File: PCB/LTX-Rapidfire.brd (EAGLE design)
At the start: 46.7 x 62.2 mm, 51 parts, among them J1 F-1X08-SIP-100-40Y, Q1 2N3904, Q10 SS8550D, Q11 2N3906, Q12 2N3906, Q13 2N3904, Q2 2N3906, Q3 2N3904, Q4 2N3904, Q5 2N3904, Q6 2N3906, Q7 2N3906, Q8 2N3906, Q9 2N3904, SW1 F-1X02-SIP-100-40

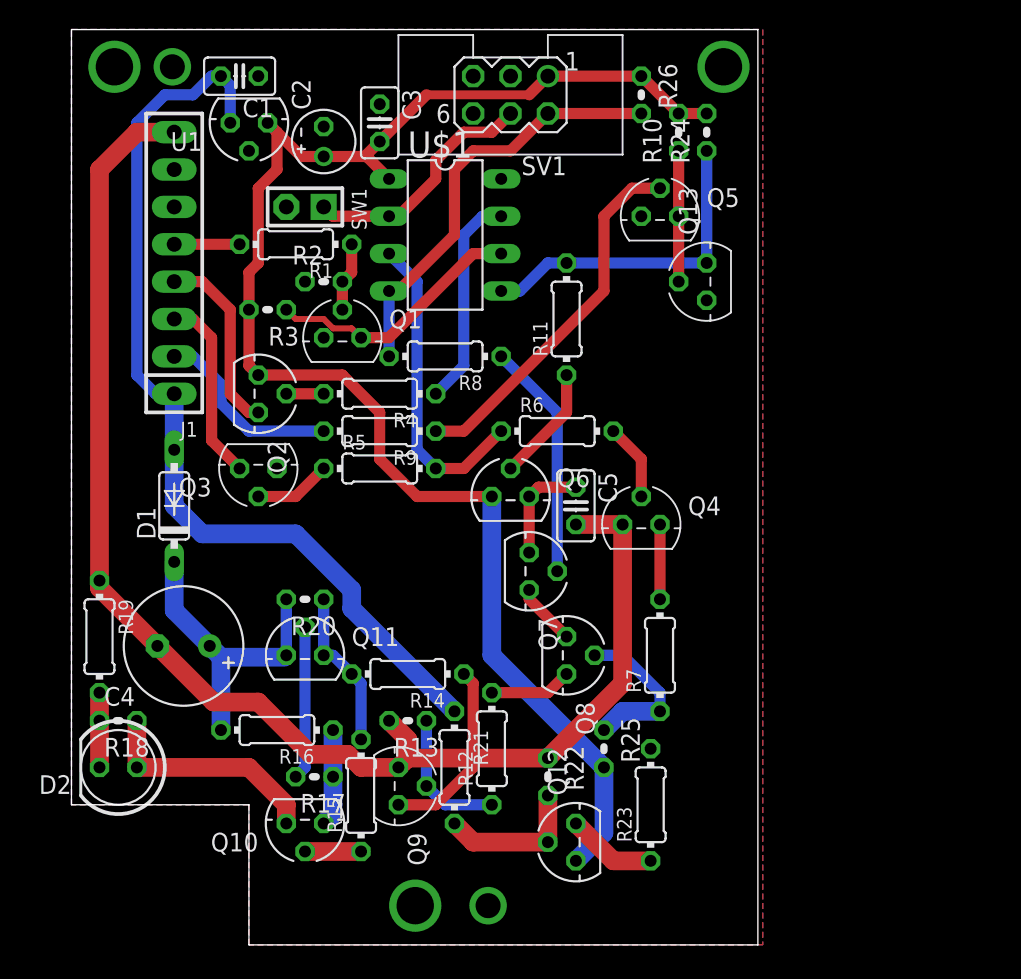
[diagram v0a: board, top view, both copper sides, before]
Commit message: Let's rotate the board so that it fits on my screen better, now that I'm not converting measurements between ExpressPCB and Eagle.
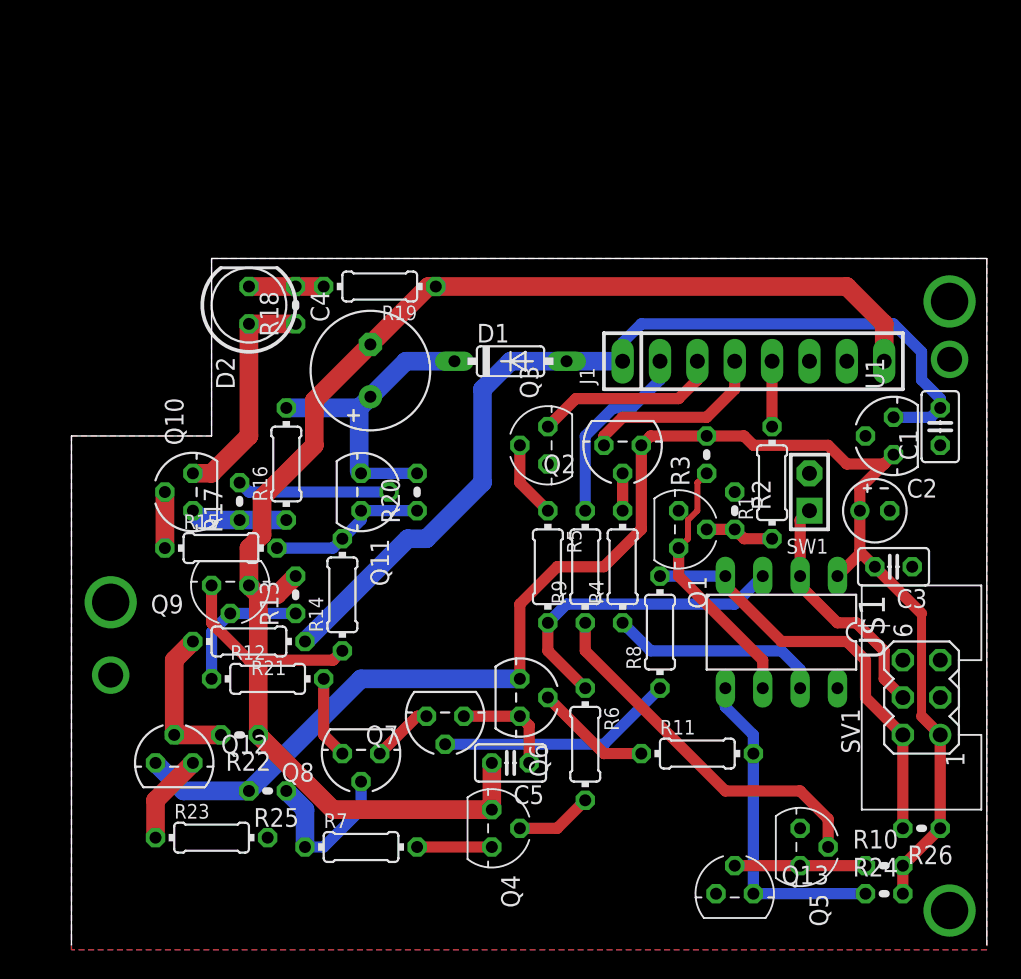
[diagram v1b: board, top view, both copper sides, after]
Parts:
- moved R26 53.4 mm to (57.8, 7.92), turned to 180 degrees
- moved C1 53.3 mm to (59.1, 35.2), turned to 90 degrees
- moved R24 53.2 mm to (55.2, 3.48), turned to 0 degrees
- moved R10 51.8 mm to (55.2, 5.38), turned to 0 degrees
- moved SV1 49.6 mm to (57.8, 16.8), turned to 90 degrees
- moved U1 48.7 mm to (55.9, 34.6), turned to 90 degrees
- moved C3 46.2 mm to (55.9, 25.7), turned to 180 degrees
- moved C2 45.1 mm to (54.6, 29.5), turned to 0 degrees
- moved Q5 43.9 mm to (49.5, 6.65), turned to 270 degrees
- moved Q13 41.6 mm to (45.1, 3.48), turned to 0 degrees
- moved J1 39.9 mm to (46.4, 39.7), turned to 0 degrees
- moved SW1 39.4 mm to (50.2, 30.8), turned to 90 degrees
- moved R1 36.2 mm to (47.6, 31.4), turned to 90 degrees
- moved U$1 35.4 mm to (48.3, 21.3), turned to 180 degrees
- moved D2 32.7 mm to (12.1, 43.5), turned to 90 degrees
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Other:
- board size 46.7 x 62.2 mm -> 62.2 x 46.7 mm

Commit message: Labels and silkscreen!
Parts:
- renumbered SV1 to J2, U$1 to U2
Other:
- board text added: "!INH"
- board text added: "(NC)"
- board text added: "LAZR"
- board text added: "PGND"
- board text added: "SGND"
- board text added: "SW9V"
- board text added: "TIDO"
- board text added: "TODI"
- board text added: "TagFerret Designs RapidBlast"
- board text added: "Version 1.0Z"
